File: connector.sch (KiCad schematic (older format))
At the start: 3 parts, among them J1 DB26_Male_HighDensity_Mountin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, SW3 SW_DIP_x03

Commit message: finalize
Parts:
- J2: renamed from J?; footprint (none) -> Connector_PinHeader_2.54mm:PinHeader_2x04_P2.54mm_Vertical
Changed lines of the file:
@@
 $Comp
 L power:GND #PWR013
-U 1 1 5F4B7169
+U 1 1 5F2D876E
 P 4525 3400
-AR Path="/5F10DACE/5F10EEE2/5F4B7169" Ref="#PWR013"  Part="1"
-AR Path="/5F1100AF/5F10EEE2/5F4B7169" Ref="#PWR?"  Part="1"
-AR Path="/5F1100FD/5F10EEE2/5F4B7169" Ref="#PWR?"  Part="1"
-AR Path="/5F110145/5F10EEE2/5F4B7169" Ref="#PWR?"  Part="1"
-AR Path="/5F11031E/5F10EEE2/5F4B7169" Ref="#PWR?"  Part="1"
-AR Path="/5F110320/5F10EEE2/5F4B7169" Ref="#PWR?"  Part="1"
-AR Path="/5F110322/5F10EEE2/5F4B7169" Ref="#PWR?"  Part="1"
-AR Path="/5F110324/5F10EEE2/5F4B7169" Ref="#PWR?"  Part="1"
-AR Path="/5F1123F9/5F10EEE2/5F4B7169" Ref="#PWR016"  Part="1"
-AR Path="/5F11264C/5F10EEE2/5F4B7169" Ref="#PWR019"  Part="1"
-AR Path="/5F11264F/5F10EEE2/5F4B7169" Ref="#PWR022"  Part="1"
-AR Path="/5F11285A/5F10EEE2/5F4B7169" Ref="#PWR025"  Part="1"
-AR Path="/5F11285D/5F10EEE2/5F4B7169" Ref="#PWR028"  Part="1"
-AR Path="/5F112860/5F10EEE2/5F4B7169" Ref="#PWR031"  Part="1"
-AR Path="/5F112863/5F10EEE2/5F4B7169" Ref="#PWR034"  Part="1"
-AR Path="/5F1F8EB1/5F4B7169" Ref="#PWR0102"  Part="1"
-AR Path="/5F202513/5F4B7169" Ref="#PWR?"  Part="1"
-AR Path="/5F214496/5F4B7169" Ref="#PWR?"  Part="1"
-AR Path="/5F2144C2/5F4B7169" Ref="#PWR?"  Part="1"
-AR Path="/5F21C578/5F4B7169" Ref="#PWR?"  Part="1"
-AR Path="/5F21C5A4/5F4B7169" Ref="#PWR?"  Part="1"
-AR Path="/5F21C5D0/5F4B7169" Ref="#PWR?"  Part="1"
-AR Path="/5F21C5FC/5F4B7169" Ref="#PWR?"  Part="1"
-AR Path="/5F22A1CE/5F4B7169" Ref="#PWR0105"  Part="1"
-AR Path="/5F22D207/5F4B7169" Ref="#PWR0108"  Part="1"
-AR Path="/5F22D233/5F4B7169" Ref="#PWR0111"  Part="1"
-AR Path="/5F2317AE/5F4B7169" Ref="#PWR0114"  Part="1"
-AR Path="/5F2317DA/5F4B7169" Ref="#PWR0117"  Part="1"
-AR Path="/5F237BED/5F4B7169" Ref="#PWR0120"  Part="1"
-AR Path="/5F237C19/5F4B7169" Ref="#PWR0123"  Part="1"
-AR Path="/5F2C117D/5F4B7169" Ref="#PWR?"  Part="1"
+AR Path="/5F10DACE/5F10EEE2/5F2D876E" Ref="#PWR013"  Part="1"
+AR Path="/5F1100AF/5F10EEE2/5F2D876E" Ref="#PWR?"  Part="1"
+AR Path="/5F1100FD/5F10EEE2/5F2D876E" Ref="#PWR?"  Part="1"
+AR Path="/5F110145/5F10EEE2/5F2D876E" Ref="#PWR?"  Part="1"
+AR Path="/5F11031E/5F10EEE2/5F2D876E" Ref="#PWR?"  Part="1"
+AR Path="/5F110320/5F10EEE2/5F2D876E" Ref="#PWR?"  Part="1"
+AR Path="/5F110322/5F10EEE2/5F2D876E" Ref="#PWR?"  Part="1"
+AR Path="/5F110324/5F10EEE2/5F2D876E" Ref="#PWR?"  Part="1"
+AR Path="/5F1123F9/5F10EEE2/5F2D876E" Ref="#PWR016"  Part="1"
+AR Path="/5F11264C/5F10EEE2/5F2D876E" Ref="#PWR019"  Part="1"
+AR Path="/5F11264F/5F10EEE2/5F2D876E" Ref="#PWR022"  Part="1"
+AR Path="/5F11285A/5F10EEE2/5F2D876E" Ref="#PWR025"  Part="1"
+AR Path="/5F11285D/5F10EEE2/5F2D876E" Ref="#PWR028"  Part="1"
+AR Path="/5F112860/5F10EEE2/5F2D876E" Ref="#PWR031"  Part="1"
+AR Path="/5F112863/5F10EEE2/5F2D876E" Ref="#PWR034"  Part="1"
+AR Path="/5F1F8EB1/5F2D876E" Ref="#PWR0102"  Part="1"
+AR Path="/5F202513/5F2D876E" Ref="#PWR?"  Part="1"
+AR Path="/5F214496/5F2D876E" Ref="#PWR?"  Part="1"
+AR Path="/5F2144C2/5F2D876E" Ref="#PWR?"  Part="1"
+AR Path="/5F21C578/5F2D876E" Ref="#PWR?"  Part="1"
+AR Path="/5F21C5A4/5F2D876E" Ref="#PWR?"  Part="1"
+AR Path="/5F21C5D0/5F2D876E" Ref="#PWR?"  Part="1"
+AR Path="/5F21C5FC/5F2D876E" Ref="#PWR?"  Part="1"
+AR Path="/5F22A1CE/5F2D876E" Ref="#PWR0105"  Part="1"
+AR Path="/5F22D207/5F2D876E" Ref="#PWR0108"  Part="1"
+AR Path="/5F22D233/5F2D876E" Ref="#PWR0111"  Part="1"
+AR Path="/5F2317AE/5F2D876E" Ref="#PWR0114"  Part="1"
+AR Path="/5F2317DA/5F2D876E" Ref="#PWR0117"  Part="1"
+AR Path="/5F237BED/5F2D876E" Ref="#PWR0120"  Part="1"
+AR Path="/5F237C19/5F2D876E" Ref="#PWR0123"  Part="1"
+AR Path="/5F2C117D/5F2D876E" Ref="#PWR?"  Part="1"
 F 0 "#PWR0105" H 4525 3150 50  0001 C CNN
 F 1 "GND" H 4530 3227 50  0000 C CNN
@@
 $Comp
 L power:GND #PWR014
-U 1 1 5F4B88F0
+U 1 1 5F2D876F
 P 5425 5300
-AR Path="/5F10DACE/5F10EEE2/5F4B88F0" Ref="#PWR014"  Part="1"
-AR Path="/5F1100AF/5F10EEE2/5F4B88F0" Ref="#PWR?"  Part="1"
-AR Path="/5F1100FD/5F10EEE2/5F4B88F0" Ref="#PWR?"  Part="1"
-AR Path="/5F110145/5F10EEE2/5F4B88F0" Ref="#PWR?"  Part="1"
-AR Path="/5F11031E/5F10EEE2/5F4B88F0" Ref="#PWR?"  Part="1"
-AR Path="/5F110320/5F10EEE2/5F4B88F0" Ref="#PWR?"  Part="1"
-AR Path="/5F110322/5F10EEE2/5F4B88F0" Ref="#PWR?"  Part="1"
-AR Path="/5F110324/5F10EEE2/5F4B88F0" Ref="#PWR?"  Part="1"
-AR Path="/5F1123F9/5F10EEE2/5F4B88F0" Ref="#PWR017"  Part="1"
-AR Path="/5F11264C/5F10EEE2/5F4B88F0" Ref="#PWR020"  Part="1"
-AR Path="/5F11264F/5F10EEE2/5F4B88F0" Ref="#PWR023"  Part="1"
-AR Path="/5F11285A/5F10EEE2/5F4B88F0" Ref="#PWR026"  Part="1"
-AR Path="/5F11285D/5F10EEE2/5F4B88F0" Ref="#PWR029"  Part="1"
-AR Path="/5F112860/5F10EEE2/5F4B88F0" Ref="#PWR032"  Part="1"
-AR Path="/5F112863/5F10EEE2/5F4B88F0" Ref="#PWR035"  Part="1"
-AR Path="/5F1F8EB1/5F4B88F0" Ref="#PWR0103"  Part="1"
-AR Path="/5F202513/5F4B88F0" Ref="#PWR?"  Part="1"
-AR Path="/5F214496/5F4B88F0" Ref="#PWR?"  Part="1"
-AR Path="/5F2144C2/5F4B88F0" Ref="#PWR?"  Part="1"
-AR Path="/5F21C578/5F4B88F0" Ref="#PWR?"  Part="1"
-AR Path="/5F21C5A4/5F4B88F0" Ref="#PWR?"  Part="1"
-AR Path="/5F21C5D0/5F4B88F0" Ref="#PWR?"  Part="1"
-AR Path="/5F21C5FC/5F4B88F0" Ref="#PWR?"  Part="1"
-AR Path="/5F22A1CE/5F4B88F0" Ref="#PWR0106"  Part="1"
-AR Path="/5F22D207/5F4B88F0" Ref="#PWR0109"  Part="1"
-AR Path="/5F22D233/5F4B88F0" Ref="#PWR0112"  Part="1"
-AR Path="/5F2317AE/5F4B88F0" Ref="#PWR0115"  Part="1"
-AR Path="/5F2317DA/5F4B88F0" Ref="#PWR0118"  Part="1"
-AR Path="/5F237BED/5F4B88F0" Ref="#PWR0121"  Part="1"
-AR Path="/5F237C19/5F4B88F0" Ref="#PWR0124"  Part="1"
-AR Path="/5F2C117D/5F4B88F0" Ref="#PWR?"  Part="1"
+AR Path="/5F10DACE/5F10EEE2/5F2D876F" Ref="#PWR014"  Part="1"
+AR Path="/5F1100AF/5F10EEE2/5F2D876F" Ref="#PWR?"  Part="1"
+AR Path="/5F1100FD/5F10EEE2/5F2D876F" Ref="#PWR?"  Part="1"
+AR Path="/5F110145/5F10EEE2/5F2D876F" Ref="#PWR?"  Part="1"
+AR Path="/5F11031E/5F10EEE2/5F2D876F" Ref="#PWR?"  Part="1"
+AR Path="/5F110320/5F10EEE2/5F2D876F" Ref="#PWR?"  Part="1"
+AR Path="/5F110322/5F10EEE2/5F2D876F" Ref="#PWR?"  Part="1"
+AR Path="/5F110324/5F10EEE2/5F2D876F" Ref="#PWR?"  Part="1"
+AR Path="/5F1123F9/5F10EEE2/5F2D876F" Ref="#PWR017"  Part="1"
+AR Path="/5F11264C/5F10EEE2/5F2D876F" Ref="#PWR020"  Part="1"
+AR Path="/5F11264F/5F10EEE2/5F2D876F" Ref="#PWR023"  Part="1"
+AR Path="/5F11285A/5F10EEE2/5F2D876F" Ref="#PWR026"  Part="1"
+AR Path="/5F11285D/5F10EEE2/5F2D876F" Ref="#PWR029"  Part="1"
+AR Path="/5F112860/5F10EEE2/5F2D876F" Ref="#PWR032"  Part="1"
+AR Path="/5F112863/5F10EEE2/5F2D876F" Ref="#PWR035"  Part="1"
+AR Path="/5F1F8EB1/5F2D876F" Ref="#PWR0103"  Part="1"
+AR Path="/5F202513/5F2D876F" Ref="#PWR?"  Part="1"
+AR Path="/5F214496/5F2D876F" Ref="#PWR?"  Part="1"
+AR Path="/5F2144C2/5F2D876F" Ref="#PWR?"  Part="1"
+AR Path="/5F21C578/5F2D876F" Ref="#PWR?"  Part="1"
+AR Path="/5F21C5A4/5F2D876F" Ref="#PWR?"  Part="1"
+AR Path="/5F21C5D0/5F2D876F" Ref="#PWR?"  Part="1"
+AR Path="/5F21C5FC/5F2D876F" Ref="#PWR?"  Part="1"
+AR Path="/5F22A1CE/5F2D876F" Ref="#PWR0106"  Part="1"
+AR Path="/5F22D207/5F2D876F" Ref="#PWR0109"  Part="1"
+AR Path="/5F22D233/5F2D876F" Ref="#PWR0112"  Part="1"
+AR Path="/5F2317AE/5F2D876F" Ref="#PWR0115"  Part="1"
+AR Path="/5F2317DA/5F2D876F" Ref="#PWR0118"  Part="1"
+AR Path="/5F237BED/5F2D876F" Ref="#PWR0121"  Part="1"
+AR Path="/5F237C19/5F2D876F" Ref="#PWR0124"  Part="1"
+AR Path="/5F2C117D/5F2D876F" Ref="#PWR?"  Part="1"
 F 0 "#PWR0106" H 5425 5050 50  0001 C CNN
 F 1 "GND" H 5430 5127 50  0000 C CNN
@@
 5V
 $Comp
-L w_connectors:HEADER_4x2 J?
+L w_connectors:HEADER_4x2 J2
 U 1 1 5F2F755E
 P 2950 4500
-F 0 "J?" H 2950 4887 60  0000 C CNN
+AR Path="/5F22A1CE/5F2F755E" Ref="J2"  Part="1"
+AR Path="/5F22D207/5F2F755E" Ref="J3"  Part="1"
+AR Path="/5F22D233/5F2F755E" Ref="J5"  Part="1"
+AR Path="/5F2317AE/5F2F755E" Ref="J7"  Part="1"
+AR Path="/5F2317DA/5F2F755E" Ref="J9"  Part="1"
+AR Path="/5F237BED/5F2F755E" Ref="J11"  Part="1"
+AR Path="/5F237C19/5F2F755E" Ref="J13"  Part="1"
+F 0 "J2" H 2950 4887 60  0000 C CNN
 F 1 "HEADER_4x2" H 2950 4781 60  0000 C CNN
-F 2 "" H 2950 4500 60  0000 C CNN
+F 2 "Connector_PinHeader_2.54mm:PinHeader_2x04_P2.54mm_Vertical" H 2950 4500 60  0001 C CNN
 F 3 "" H 2950 4500 60  0000 C CNN
 	1    2950 4500

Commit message: Switch to female footprints and update positionning
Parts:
- J1: footprint DB-HD-26:DSUB-26-HD_Male_Horizontal_P2.29x1.98mm_EdgePinOffset8.35mm_Housed_MountingHolesOffset10.89mm -> Connector_Dsub:DSUB-26-HD_Female_Horizontal_P2.29x1.98mm_EdgePinOffset3.03mm_Housed_MountingHolesOffset4.94mm
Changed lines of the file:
@@
 F 0 "J4" H 5425 6217 50  0000 C CNN
 F 1 "DB26_Male_HighDensity_MountingHoles" H 5425 6126 50  0000 C CNN
-F 2 "DB-HD-26:DSUB-26-HD_Male_Horizontal_P2.29x1.98mm_EdgePinOffset8.35mm_Housed_MountingHolesOffset10.89mm" H 4475 5000 50  0001 C CNN
+F 2 "Connector_Dsub:DSUB-26-HD_Female_Horizontal_P2.29x1.98mm_EdgePinOffset3.03mm_Housed_MountingHolesOffset4.94mm" H 4475 5000 50  0001 C CNN
 F 3 "https://www.mouser.fr/ProductDetail/Kycon/K66X-A26S-N?qs=C%252BuF95oynlmx3ziDhlO2Bg%3D%3D" H 4475 5000 50  0001 C CNN
 	1    5425 4600

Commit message: New layout with FPGA
- Added FPGA to ease UART and SPI signals routing
- Cleaned layout using start and circle patterns for remaining signals
- Replaced DCDC modules with better TI components

Missing stuff:
- per module PSU switch
- spare FPGA IOs connector?
- silk screen
- ...

Signed-off-by: Alexis Jeandet <alexis.jeandet@member.fsf.org>
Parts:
- removed J2: HEADER_4x2, Connector_PinHeader_2.54mm:PinHeader_2x04_P2.54mm_Vertical, symbol w_connectors:HEADER_4x2
- removed SW3: SW_DIP_x03, Button_Switch_THT:SW_DIP_SPSTx03_Slide_9.78x9.8mm_W7.62mm_P2.54mm, symbol Switch:SW_DIP_x03
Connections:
- net labels removed: OBC_UART1_RX, OBC_UART1_TX, OBC_UART2_RX, OBC_UART2_TX
- wire segments 28 -> 20
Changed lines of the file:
@@
 $Descr A4 11693 8268
 encoding utf-8
-Sheet 2 9
+Sheet 7 15
 Title ""
 Date ""
@@
 AR Path="/5F237C19/5F14DCB5" Ref="J16"  Part="1"
 AR Path="/5F2C117D/5F14DCB5" Ref="J?"  Part="1"
-F 0 "J4" H 5425 6217 50  0000 C CNN
+AR Path="/5F66A269/5F14DCB5" Ref="J5"  Part="1"
+F 0 "J14" H 5425 6217 50  0000 C CNN
 F 1 "DB26_Male_HighDensity_MountingHoles" H 5425 6126 50  0000 C CNN
 F 2 "Connector_Dsub:DSUB-26-HD_Female_Horizontal_P2.29x1.98mm_EdgePinOffset3.03mm_Housed_MountingHolesOffset4.94mm" H 4475 5000 50  0001 C CNN
@@
 Wire Wire Line
 	5125 5000 4725 5000
-Text Label 4725 3900 2    50   ~ 0
-UART2_RX
-Text Label 6125 3900 0    50   ~ 0
-UART2_TX
-Text Label 4725 4000 2    50   ~ 0
-UART1_TX
-Text Label 6125 4100 0    50   ~ 0
-UART1_RX
 Wire Wire Line
 	5125 3400 4525 3400
@@
 AR Path="/5F237C19/5F2D876E" Ref="#PWR0123"  Part="1"
 AR Path="/5F2C117D/5F2D876E" Ref="#PWR?"  Part="1"
-F 0 "#PWR0105" H 4525 3150 50  0001 C CNN
+AR Path="/5F66A269/5F2D876E" Ref="#PWR064"  Part="1"
+F 0 "#PWR064" H 4525 3150 50  0001 C CNN
 F 1 "GND" H 4530 3227 50  0000 C CNN
 F 2 "" H 4525 3400 50  0001 C CNN
@@
 AR Path="/5F237C19/5F2D876F" Ref="#PWR0124"  Part="1"
 AR Path="/5F2C117D/5F2D876F" Ref="#PWR?"  Part="1"
-F 0 "#PWR0106" H 5425 5050 50  0001 C CNN
+AR Path="/5F66A269/5F2D876F" Ref="#PWR065"  Part="1"
+F 0 "#PWR065" H 5425 5050 50  0001 C CNN
 F 1 "GND" H 5430 5127 50  0000 C CNN
 F 2 "" H 5425 5300 50  0001 C CNN
 F 3 "" H 5425 5300 50  0001 C CNN
 	1    5425 5300
-	1    0    0    -1
-$EndComp
-$Comp
-L Switch:SW_DIP_x03 SW3
-U 1 1 5F14E492
-P 2975 3575
-AR Path="/5F1123F9/5F10EEE2/5F14E492" Ref="SW3"  Part="1"
-AR Path="/5F11264C/5F10EEE2/5F14E492" Ref="SW4"  Part="1"
-AR Path="/5F10DACE/5F10EEE2/5F14E492" Ref="SW2"  Part="1"
-AR Path="/5F11264F/5F10EEE2/5F14E492" Ref="SW5"  Part="1"
-AR Path="/5F11285A/5F10EEE2/5F14E492" Ref="SW6"  Part="1"
-AR Path="/5F11285D/5F10EEE2/5F14E492" Ref="SW7"  Part="1"
-AR Path="/5F112860/5F10EEE2/5F14E492" Ref="SW8"  Part="1"
-AR Path="/5F112863/5F10EEE2/5F14E492" Ref="SW9"  Part="1"
-AR Path="/5F1F8EB1/5F14E492" Ref="SW2"  Part="1"
-AR Path="/5F202513/5F14E492" Ref="SW?"  Part="1"
-AR Path="/5F214496/5F14E492" Ref="SW?"  Part="1"
-AR Path="/5F2144C2/5F14E492" Ref="SW?"  Part="1"
-AR Path="/5F21C578/5F14E492" Ref="SW?"  Part="1"
-AR Path="/5F21C5A4/5F14E492" Ref="SW?"  Part="1"
-AR Path="/5F21C5D0/5F14E492" Ref="SW?"  Part="1"
-AR Path="/5F21C5FC/5F14E492" Ref="SW?"  Part="1"
-AR Path="/5F22A1CE/5F14E492" Ref="SW3"  Part="1"
-AR Path="/5F22D207/5F14E492" Ref="SW4"  Part="1"
-AR Path="/5F22D233/5F14E492" Ref="SW5"  Part="1"
-AR Path="/5F2317AE/5F14E492" Ref="SW6"  Part="1"
-AR Path="/5F2317DA/5F14E492" Ref="SW7"  Part="1"
-AR Path="/5F237BED/5F14E492" Ref="SW8"  Part="1"
-AR Path="/5F237C19/5F14E492" Ref="SW9"  Part="1"
-AR Path="/5F2C117D/5F14E492" Ref="SW?"  Part="1"
-F 0 "SW3" H 2975 4042 50  0000 C CNN
-F 1 "SW_DIP_x03" H 2975 3951 50  0000 C CNN
-F 2 "Button_Switch_THT:SW_DIP_SPSTx03_Slide_9.78x9.8mm_W7.62mm_P2.54mm" H 2975 3575 50  0001 C CNN
-F 3 "~" H 2975 3575 50  0001 C CNN
-	1    2975 3575
 	1    0    0    -1
 $EndComp
@@
 Text GLabel 2675 3575 0    50   Input ~ 0
 5V
-$Comp
-L w_connectors:HEADER_4x2 J2
-U 1 1 5F2F755E
-P 2950 4500
-AR Path="/5F22A1CE/5F2F755E" Ref="J2"  Part="1"
-AR Path="/5F22D207/5F2F755E" Ref="J3"  Part="1"
-AR Path="/5F22D233/5F2F755E" Ref="J5"  Part="1"
-AR Path="/5F2317AE/5F2F755E" Ref="J7"  Part="1"
-AR Path="/5F2317DA/5F2F755E" Ref="J9"  Part="1"
-AR Path="/5F237BED/5F2F755E" Ref="J11"  Part="1"
-AR Path="/5F237C19/5F2F755E" Ref="J13"  Part="1"
-F 0 "J2" H 2950 4887 60  0000 C CNN
-F 1 "HEADER_4x2" H 2950 4781 60  0000 C CNN
-F 2 "Connector_PinHeader_2.54mm:PinHeader_2x04_P2.54mm_Vertical" H 2950 4500 60  0001 C CNN
-F 3 "" H 2950 4500 60  0000 C CNN
-	1    2950 4500
-	1    0    0    -1
-$EndComp
-Wire Wire Line
-	2800 4350 2500 4350
-Wire Wire Line
-	2800 4450 2500 4450
-Wire Wire Line
-	2800 4550 2500 4550
-Wire Wire Line
-	2800 4650 2500 4650
-Text Label 2500 4350 2    50   ~ 0
+Text HLabel 4725 3900 0    50   Input ~ 0
+UART2_RX
+Text HLabel 4725 4000 0    50   Input ~ 0
+UART1_TX
+Text HLabel 6125 3900 2    50   Input ~ 0
+UART2_TX
+Text HLabel 6125 4100 2    50   Input ~ 0
 UART1_RX
-Text Label 2500 4450 2    50   ~ 0
-UART1_TX
-Text Label 2500 4550 2    50   ~ 0
-UART2_RX
-Text Label 2500 4650 2    50   ~ 0
-UART2_TX
-Wire Wire Line
-	3400 4350 3100 4350
-Wire Wire Line
-	3400 4450 3100 4450
-Wire Wire Line
-	3400 4550 3100 4550
-Wire Wire Line
-	3400 4650 3100 4650
-Text GLabel 3400 4350 2    50   Input ~ 0
-OBC_UART1_TX
-Text GLabel 3400 4450 2    50   Input ~ 0
-OBC_UART1_RX
-Text GLabel 3400 4550 2    50   Input ~ 0
-OBC_UART2_TX
-Text GLabel 3400 4650 2    50   Input ~ 0
-OBC_UART2_RX
 $EndSCHEMATC

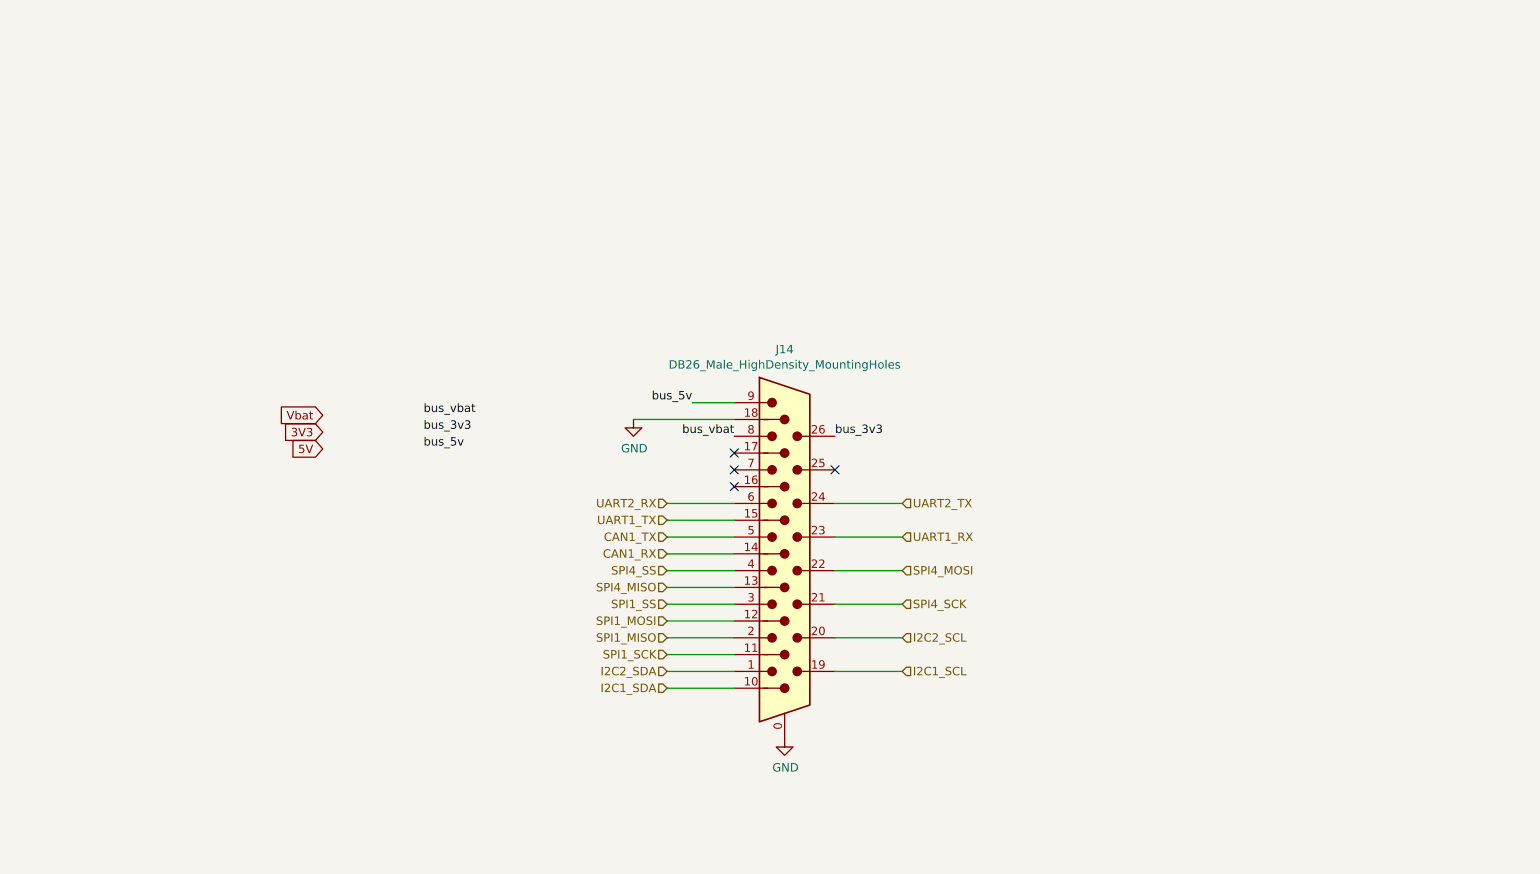
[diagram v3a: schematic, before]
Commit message: Most PSB done, needs more silk screen cosmetic plus review
Signed-off-by: Alexis Jeandet <alexis.jeandet@member.fsf.org>
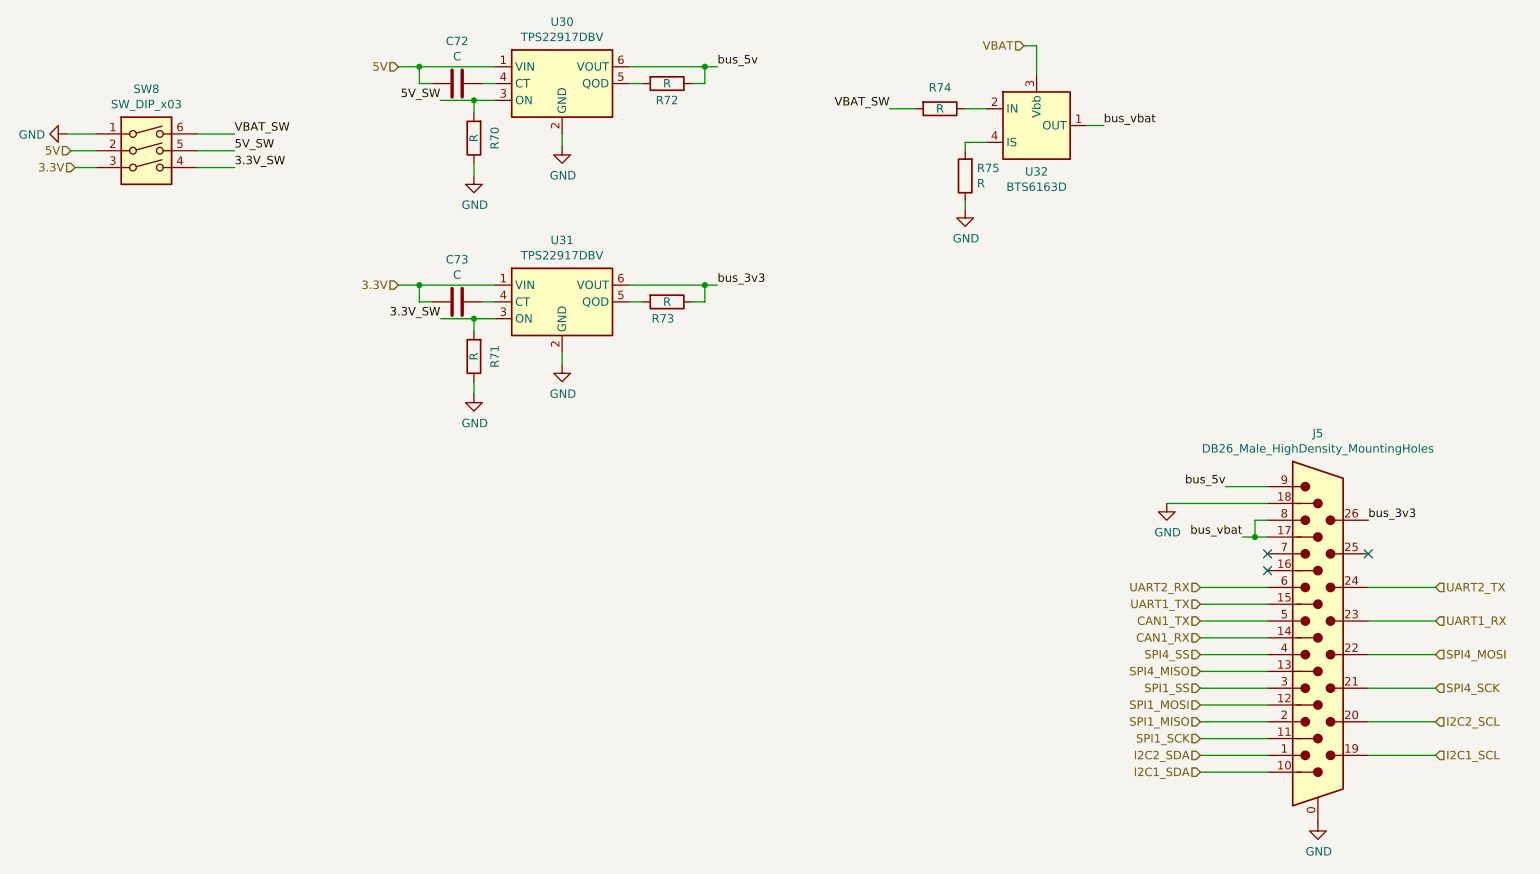
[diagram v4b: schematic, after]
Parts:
- added C60, C61: C, Capacitor_SMD:C_0603_1608Metric_Pad1.05x0.95mm_HandSolder, symbol Device:C
- added R34, R35, R38, R39: R, Resistor_SMD:R_0603_1608Metric_Pad1.05x0.95mm_HandSolder, symbol Device:R
- added R36, R37: R, Resistor_SMD:R_1210_3225Metric_Pad1.42x2.65mm_HandSolder, symbol Device:R
- added SW2: SW_DIP_x03, Button_Switch_THT:SW_DIP_SPSTx03_Slide_9.78x9.8mm_W7.62mm_P2.54mm, symbol Switch:SW_DIP_x03
- added U12, U13: TPS22917DBV, Package_TO_SOT_SMD:SOT-23-6, symbol Power_Management:TPS22917DBV
- added U14: BTS6163D, Package_TO_SOT_SMD:TO-252-4, symbol Power_Management:BTS6163D
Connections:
- net 5V: now also C60.2, SW2.2, U12.1 (VIN)
- net GND: now also R34.1, R35.1, R39.1, SW2.1, U12.2 (GND), U13.2 (GND)
- net bus_3v3: now also R37.1, U13.6 (VOUT)
- net bus_5v: now also R36.1, U12.6 (VOUT)
- net bus_vbat: now also J1.17, U14.1 (OUT), U14.5 (OUT)
- new net: R38.1, U14.2 (IN)
- new net: R39.2, U14.4 (IS)
- new net: C60.1, U12.4 (CT)
- new net: R36.2, U12.5 (QOD)
- new net: C61.1, U13.4 (CT)
- new net: R37.2, U13.5 (QOD)
- new net 3.3V: C61.2, SW2.3, U13.1 (VIN)
- new net 3.3V_SW: R35.2, SW2.4, U13.3 (ON)
- new net 5V_SW: R34.2, SW2.5, U12.3 (ON)
- new net VBAT: U14.3 (Vbb)
- new net VBAT_SW: R38.2, SW2.6
- no-connect marks 4 -> 3
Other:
- moved on the sheet: J5
